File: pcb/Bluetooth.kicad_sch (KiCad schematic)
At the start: 22 parts, among them U12 74HC2G14, U13 74HC2G14, U14 RN4678

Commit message: [pcb] Voltage regulator changed to TLV761
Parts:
- C25: footprint Capacitor_Tantalum_SMD:CP_EIA-3528-12_Kemet-T -> Capacitor_Tantalum_SMD:CP_EIA-3216-18_Kemet-A
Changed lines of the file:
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@@
       (effects (font (size 1.27 1.27)) (justify left))
     )
-    (property "Footprint" "Capacitor_Tantalum_SMD:CP_EIA-3528-12_Kemet-T" (at 25.7048 54.61 0)
+    (property "Footprint" "Capacitor_Tantalum_SMD:CP_EIA-3216-18_Kemet-A" (at 25.7048 54.61 0)
       (effects (font (size 1.27 1.27)) hide)
     )

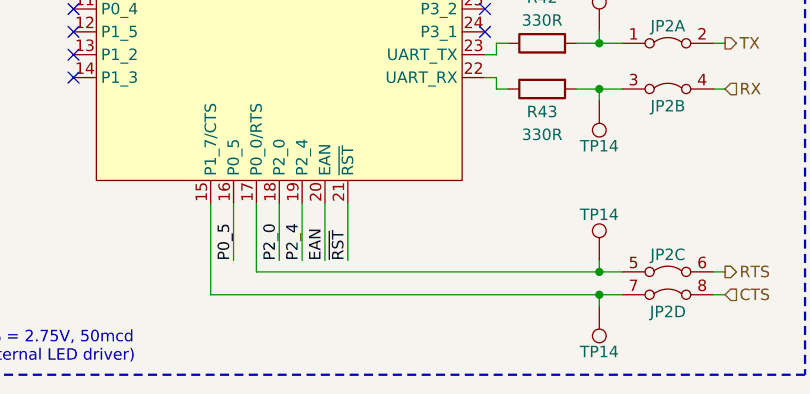
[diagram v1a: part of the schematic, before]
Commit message: [pcb] Test points reduced to 1.5mm; flow control series resistors added
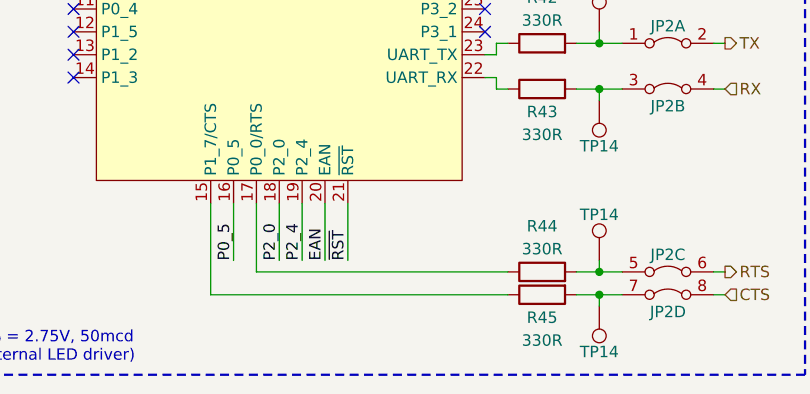
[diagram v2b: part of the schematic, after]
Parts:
- added R44, R45: 330R, Resistor_SMD:R_0805_2012Metric, symbol Device:R
- TP14: footprint TestPoint:TestPoint_Pad_D2.0mm -> TestPoint:TestPoint_Pad_D1.5mm
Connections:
- net at JP2.7, TP14.1: now also R45.2; no longer U14.15 (P1_7/CTS)
- net at JP2.5, TP14.1: now also R44.2; no longer U14.17 (P0_0/RTS)
- new net: R45.1, U14.15 (P1_7/CTS)
- new net: R44.1, U14.17 (P0_0/RTS)

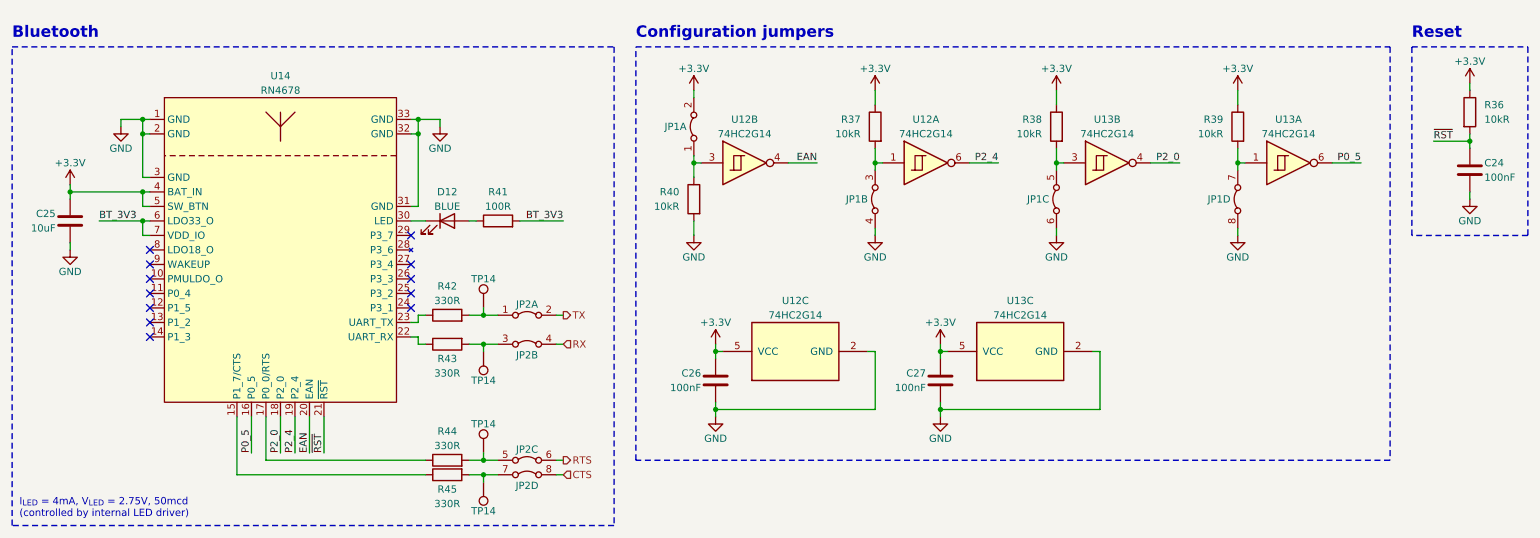
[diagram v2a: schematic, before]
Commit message: [pcb] Rename line sensors to S1..S7
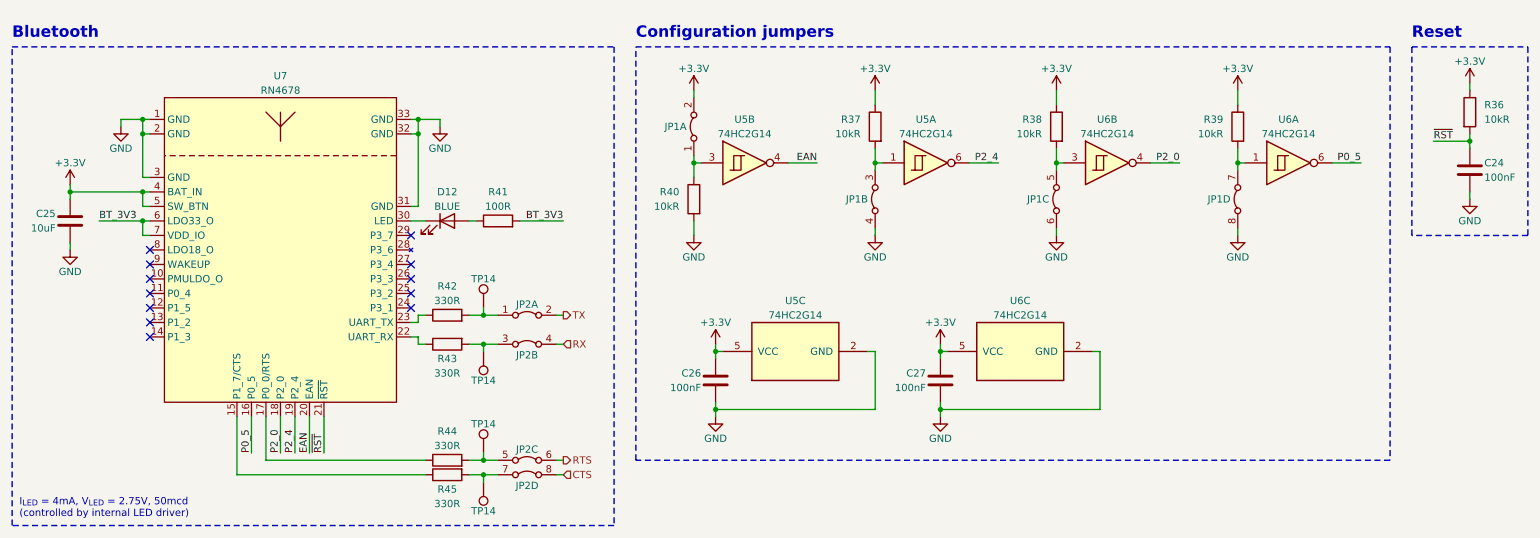
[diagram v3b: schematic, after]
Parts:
- renumbered U12 to U5, U13 to U6, U14 to U7
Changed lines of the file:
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@@
   (symbol (lib_id "Autko:74HC2G14") (at 193.04 73.66 90) (unit 3)
     (in_bom yes) (on_board yes) (dnp no) (fields_autoplaced)
-    (property "Reference" "U13" (at 193.04 64.77 90)
+    (property "Reference" "U6" (at 193.04 64.77 90)
       (effects (font (size 1.27 1.27)))
     )
@@
       (project "Autko"
         (path "/8d5cfdec-de34-4148-9100-7125640c46f5/bb9a200c-6921-438f-a82b-708524bb5612"
-          (reference "U13") (unit 3)
+          (reference "U6") (unit 3)
         )
       )
@@
   (symbol (lib_id "Autko:74HC2G14") (at 208.28 40.64 0) (unit 2)
     (in_bom yes) (on_board yes) (dnp no) (fields_autoplaced)
-    (property "Reference" "U13" (at 208.28 33.02 0)
+    (property "Reference" "U6" (at 208.28 33.02 0)
       (effects (font (size 1.27 1.27)))
     )
@@
       (project "Autko"
         (path "/8d5cfdec-de34-4148-9100-7125640c46f5/bb9a200c-6921-438f-a82b-708524bb5612"
-          (reference "U13") (unit 2)
+          (reference "U6") (unit 2)
         )
       )
@@
   (symbol (lib_id "Autko:RN4678") (at 63.5 55.88 0) (unit 1)
     (in_bom yes) (on_board yes) (dnp no) (fields_autoplaced)
-    (property "Reference" "U14" (at 63.5 25.4 0)
+    (property "Reference" "U7" (at 63.5 25.4 0)
       (effects (font (size 1.27 1.27)))
     )
@@
       (project "Autko"
         (path "/8d5cfdec-de34-4148-9100-7125640c46f5/bb9a200c-6921-438f-a82b-708524bb5612"
-          (reference "U14") (unit 1)
+          (reference "U7") (unit 1)
         )
       )
@@
   (symbol (lib_id "Autko:74HC2G14") (at 144.78 40.64 0) (unit 2)
     (in_bom yes) (on_board yes) (dnp no) (fields_autoplaced)
-    (property "Reference" "U12" (at 144.78 33.02 0)
+    (property "Reference" "U5" (at 144.78 33.02 0)
       (effects (font (size 1.27 1.27)))
     )
@@
       (project "Autko"
         (path "/8d5cfdec-de34-4148-9100-7125640c46f5/bb9a200c-6921-438f-a82b-708524bb5612"
-          (reference "U12") (unit 2)
+          (reference "U5") (unit 2)
         )
       )
@@
   (symbol (lib_id "Autko:74HC2G14") (at 176.53 40.64 0) (unit 1)
     (in_bom yes) (on_board yes) (dnp no) (fields_autoplaced)
-    (property "Reference" "U12" (at 176.53 33.02 0)
+    (property "Reference" "U5" (at 176.53 33.02 0)
       (effects (font (size 1.27 1.27)))
     )
@@
       (project "Autko"
         (path "/8d5cfdec-de34-4148-9100-7125640c46f5/bb9a200c-6921-438f-a82b-708524bb5612"
-          (reference "U12") (unit 1)
+          (reference "U5") (unit 1)
         )
       )
@@
   (symbol (lib_id "Autko:74HC2G14") (at 240.03 40.64 0) (unit 1)
     (in_bom yes) (on_board yes) (dnp no) (fields_autoplaced)
-    (property "Reference" "U13" (at 240.03 33.02 0)
+    (property "Reference" "U6" (at 240.03 33.02 0)
       (effects (font (size 1.27 1.27)))
     )
@@
       (project "Autko"
         (path "/8d5cfdec-de34-4148-9100-7125640c46f5/bb9a200c-6921-438f-a82b-708524bb5612"
-          (reference "U13") (unit 1)
+          (reference "U6") (unit 1)
         )
       )
@@
   (symbol (lib_id "Autko:74HC2G14") (at 153.67 73.66 90) (unit 3)
     (in_bom yes) (on_board yes) (dnp no) (fields_autoplaced)
-    (property "Reference" "U12" (at 153.67 64.77 90)
+    (property "Reference" "U5" (at 153.67 64.77 90)
       (effects (font (size 1.27 1.27)))
     )
@@
       (project "Autko"
         (path "/8d5cfdec-de34-4148-9100-7125640c46f5/bb9a200c-6921-438f-a82b-708524bb5612"
-          (reference "U12") (unit 3)
-        )
-      )
+          (reference "U5") (unit 3)
+        )
+      )

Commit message: [pcb] Bluetooth configuration simplified
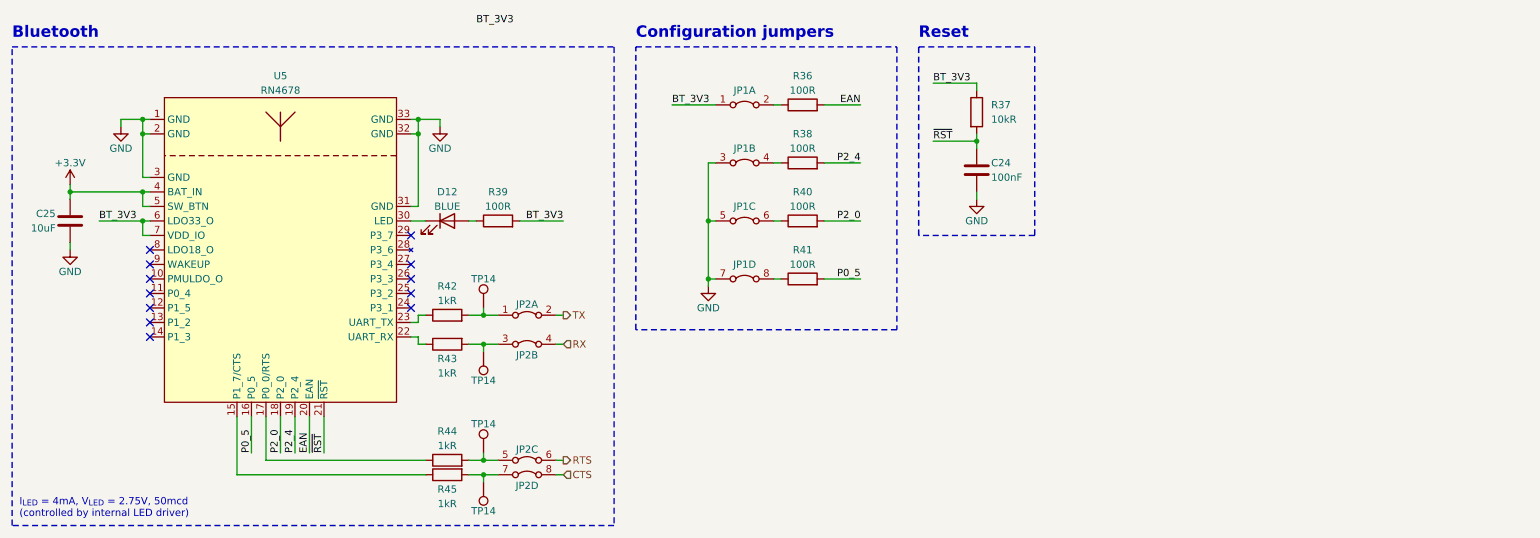
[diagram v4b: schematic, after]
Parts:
- removed C26, C27: 100nF, Capacitor_SMD:C_0805_2012Metric, symbol Device:C
- removed R37, R39: 10kR, Resistor_SMD:R_0805_2012Metric, symbol Device:R
- removed U5, U6: 74HC2G14, Package_TO_SOT_SMD:SOT-363_SC-70-6, symbol Autko:74HC2G14
- added R36, R41: 100R, Resistor_SMD:R_0805_2012Metric, symbol Device:R
- R38, R40: value 10kR -> 100R
- R42, R43, R44, R45: value 330R -> 1kR
- renumbered R36 to R37, R41 to R39, U7 to U5
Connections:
- net +3.3V: no longer JP1.2, R37.1, R38.1
- net BT_3V3: now also JP1.1, R37.1
- net EAN: now also R36.2
- net GND: now also JP1.3, JP1.5, JP1.7; no longer JP1.4, JP1.6, JP1.8, R40.2
- net P0_5: now also R41.2
- net P2_0: now also R40.2
- net P2_4: now also R38.2
- net at R40.1: now also JP1.6; no longer JP1.1
- new net: JP1.4, R38.1
- new net: JP1.2, R36.1
- new net: JP1.8, R41.1
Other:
- moved on the sheet: C24, JP1A, JP1B, JP1C, JP1D, R37

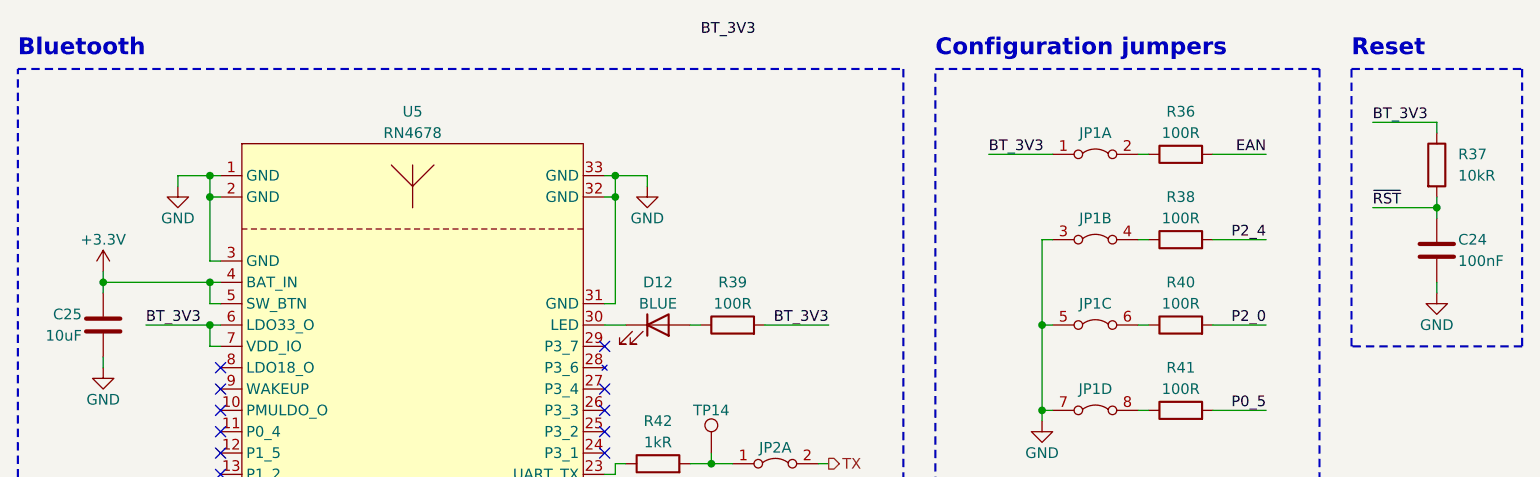
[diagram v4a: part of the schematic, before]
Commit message: [pcb] Assign smaller footprints
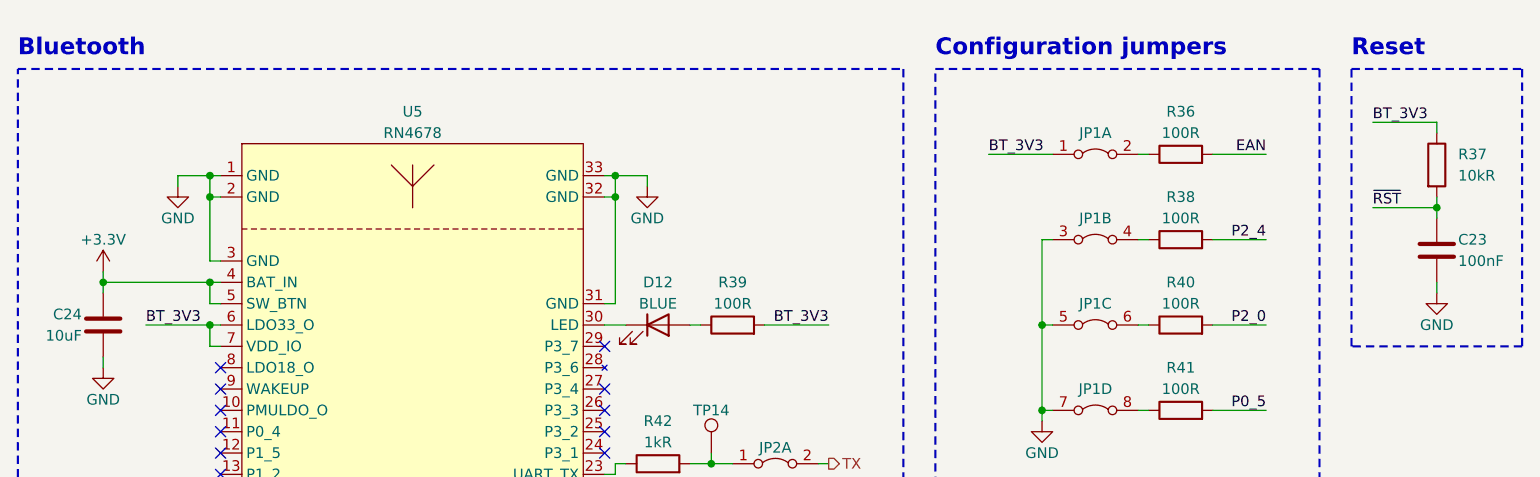
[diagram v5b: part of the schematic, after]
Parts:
- C23: renamed from C24; footprint Capacitor_SMD:C_0805_2012Metric -> Capacitor_SMD:C_0603_1608Metric
- C24: renamed from C25; footprint Capacitor_Tantalum_SMD:CP_EIA-3216-18_Kemet-A -> Capacitor_SMD:C_1206_3216Metric
- D12: footprint LED_SMD:LED_0805_2012Metric -> LED_SMD:LED_0603_1608Metric
- R36, R37, R38, R39, R40, R41, R42, R43, R44, R45: footprint Resistor_SMD:R_0805_2012Metric -> Resistor_SMD:R_0603_1608Metric
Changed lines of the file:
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@@
     (effects (font (size 2 2) (thickness 0.4) bold) (justify left bottom))
-  )
-  (label "BT_3V3" (at 97.79 16.51 0) (fields_autoplaced)
-    (effects (font (size 1.27 1.27)) (justify left bottom))
   )
   (label "BT_3V3" (at 132.08 30.48 0) (fields_autoplaced)
@@
       (effects (font (size 1.27 1.27)))
     )
-    (property "Footprint" "Resistor_SMD:R_0805_2012Metric" (at 101.6 52.578 90)
+    (property "Footprint" "Resistor_SMD:R_0603_1608Metric" (at 101.6 52.578 90)
       (effects (font (size 1.27 1.27)) hide)
     )
@@
       (effects (font (size 1.27 1.27)))
     )
-    (property "Footprint" "Resistor_SMD:R_0805_2012Metric" (at 92.71 70.612 90)
+    (property "Footprint" "Resistor_SMD:R_0603_1608Metric" (at 92.71 70.612 90)
       (effects (font (size 1.27 1.27)) hide)
     )
@@
       (effects (font (size 1.27 1.27)))
     )
-    (property "Footprint" "Resistor_SMD:R_0805_2012Metric" (at 154.94 32.258 90)
+    (property "Footprint" "Resistor_SMD:R_0603_1608Metric" (at 154.94 32.258 90)
       (effects (font (size 1.27 1.27)) hide)
     )
@@
       (effects (font (size 1.27 1.27)))
     )
-    (property "Footprint" "LED_SMD:LED_0805_2012Metric" (at 92.71 50.8 0)
+    (property "Footprint" "LED_SMD:LED_0603_1608Metric" (at 92.71 50.8 0)
       (effects (font (size 1.27 1.27)) hide)
     )
@@
   (symbol (lib_id "Device:C") (at 185.42 41.91 0) (unit 1)
     (in_bom yes) (on_board yes) (dnp no)
-    (property "Reference" "C24" (at 187.96 40.64 0)
+    (property "Reference" "C23" (at 187.96 40.64 0)
       (effects (font (size 1.27 1.27)) (justify left))
     )
@@
       (effects (font (size 1.27 1.27)) (justify left))
     )
-    (property "Footprint" "Capacitor_SMD:C_0805_2012Metric" (at 186.3852 45.72 0)
+    (property "Footprint" "Capacitor_SMD:C_0603_1608Metric" (at 186.3852 45.72 0)
       (effects (font (size 1.27 1.27)) hide)
     )
@@
       (project "Autko"
         (path "/8d5cfdec-de34-4148-9100-7125640c46f5/bb9a200c-6921-438f-a82b-708524bb5612"
-          (reference "C24") (unit 1)
+          (reference "C23") (unit 1)
         )
       )
@@
       (effects (font (size 1.27 1.27)))
     )
-    (property "Footprint" "Resistor_SMD:R_0805_2012Metric" (at 92.71 93.472 90)
+    (property "Footprint" "Resistor_SMD:R_0603_1608Metric" (at 92.71 93.472 90)
       (effects (font (size 1.27 1.27)) hide)
     )
@@
       (effects (font (size 1.27 1.27)) (justify left))
     )
-    (property "Footprint" "Resistor_SMD:R_0805_2012Metric" (at 183.642 31.75 90)
+    (property "Footprint" "Resistor_SMD:R_0603_1608Metric" (at 183.642 31.75 90)
       (effects (font (size 1.27 1.27)) hide)
     )
@@
       (effects (font (size 1.27 1.27)))
     )
-    (property "Footprint" "Resistor_SMD:R_0805_2012Metric" (at 154.94 62.738 90)
+    (property "Footprint" "Resistor_SMD:R_0603_1608Metric" (at 154.94 62.738 90)
       (effects (font (size 1.27 1.27)) hide)
     )
@@
   (symbol (lib_id "Device:C") (at 26.67 50.8 0) (mirror y) (unit 1)
     (in_bom yes) (on_board yes) (dnp no)
-    (property "Reference" "C25" (at 24.13 49.53 0)
+    (property "Reference" "C24" (at 24.13 49.53 0)
       (effects (font (size 1.27 1.27)) (justify left))
     )
@@
       (effects (font (size 1.27 1.27)) (justify left))
     )
-    (property "Footprint" "Capacitor_Tantalum_SMD:CP_EIA-3216-18_Kemet-A" (at 25.7048 54.61 0)
+    (property "Footprint" "Capacitor_SMD:C_1206_3216Metric" (at 25.7048 54.61 0)
       (effects (font (size 1.27 1.27)) hide)
     )
@@
       (project "Autko"
         (path "/8d5cfdec-de34-4148-9100-7125640c46f5/bb9a200c-6921-438f-a82b-708524bb5612"
-          (reference "C25") (unit 1)
+          (reference "C24") (unit 1)
         )
       )
@@
       (effects (font (size 1.27 1.27)))
     )
-    (property "Footprint" "Resistor_SMD:R_0805_2012Metric" (at 154.94 42.418 90)
+    (property "Footprint" "Resistor_SMD:R_0603_1608Metric" (at 154.94 42.418 90)
       (effects (font (size 1.27 1.27)) hide)
     )
@@
       (effects (font (size 1.27 1.27)))
     )
-    (property "Footprint" "Resistor_SMD:R_0805_2012Metric" (at 92.71 94.488 90)
+    (property "Footprint" "Resistor_SMD:R_0603_1608Metric" (at 92.71 94.488 90)
       (effects (font (size 1.27 1.27)) hide)
     )
@@
       (effects (font (size 1.27 1.27)))
     )
-    (property "Footprint" "Resistor_SMD:R_0805_2012Metric" (at 92.71 69.088 90)
+    (property "Footprint" "Resistor_SMD:R_0603_1608Metric" (at 92.71 69.088 90)
       (effects (font (size 1.27 1.27)) hide)
     )
@@
       (effects (font (size 1.27 1.27)))
     )
-    (property "Footprint" "Resistor_SMD:R_0805_2012Metric" (at 154.94 52.578 90)
-      (effects (font (size 1.27 1.27)) hide)
-    )
+    (property "Footprint" "Resistor_SMD:R_0603_1608Metric" (at 154.94 52.578 90)
+      (effects (font (size 1.27 1.27)) hide)
+    )
